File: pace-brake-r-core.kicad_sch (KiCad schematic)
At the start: 15 parts, among them Q1 AOD4184, Q2 AOD4184, U1 EG2131, U2 TL432AIDBZR

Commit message: updated notes in schematic
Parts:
- C1: footprint (none) -> Capacitor_SMD:C_0402_1005Metric
- D2: footprint (none) -> LED_SMD:LED_0805_2012Metric
- R1, R2, R3, R5, R6: footprint (none) -> Resistor_SMD:R_0402_1005Metric
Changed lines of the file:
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@@
 	)
 	(image
-		(at 146.05 27.94)
+		(at 142.24 -15.24)
 		(data "iVBORw0KGgoAAAANSUhEUgAACjsAAAP9CAYAAADR000DAAAABHNCSVQICAgIfAhkiAAAIABJREFU"
 			"eJzs3emXbFd55/nfs88QkXdEQkgIhEGAJYEE2MYYbLDAgO0qXMYuqHJNtld3Vy/36nrXq1cPf0S/"
@@
 	)
 	(image
-		(at -8.89 127)
+		(at -48.26 57.15)
 		(data "iVBORw0KGgoAAAANSUhEUgAAA7oAAAJ9CAYAAAAbng7VAAAABHNCSVQICAgIfAhkiAAAIABJREFU"
 			"eJzs3X9YVHXe//EXijoU5GC2DZspmFaYlrB2Kaxed2CtOebeBrfuBumWo96rWHsX6Fa6fnddrE2l"
@@
 			)
 		)
-		(property "Footprint" ""
+		(property "Footprint" "Resistor_SMD:R_0402_1005Metric"
 			(at 64.516 122.174 90)
 			(hide yes)
@@
 			)
 		)
-		(property "Footprint" ""
+		(property "Footprint" "LED_SMD:LED_0805_2012Metric"
 			(at 238.76 113.03 0)
 			(hide yes)
@@
 			)
 		)
-		(property "Footprint" ""
+		(property "Footprint" "Resistor_SMD:R_0402_1005Metric"
 			(at 162.814 129.794 90)
 			(hide yes)
@@
 			)
 		)
-		(property "Footprint" ""
+		(property "Footprint" "Resistor_SMD:R_0402_1005Metric"
 			(at 117.094 159.004 90)
 			(hide yes)
@@
 			)
 		)
-		(property "Footprint" ""
+		(property "Footprint" "Resistor_SMD:R_0402_1005Metric"
 			(at 226.314 127.254 90)
 			(hide yes)
@@
 			)
 		)
-		(property "Footprint" ""
+		(property "Footprint" "Resistor_SMD:R_0402_1005Metric"
 			(at 92.456 122.174 90)
 			(hide yes)
@@
 			)
 		)
-		(property "Footprint" ""
+		(property "Footprint" "Capacitor_SMD:C_0402_1005Metric"
 			(at 129.54 109.22 0)
 			(hide yes)

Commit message: Last version with LED indicator
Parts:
- removed D1: MBRD30100CT, imported-project-library:TO-252-2_L6.6-W6.1-P4.57-LS9.9-BR-CW, symbol imported-project-library:MBRD30100CT
- removed R7: ~, symbol Device:R
- added C16: 33nF, Capacitor_SMD:C_0402_1005Metric, symbol Device:C_Small
- added C17: 100uF 16v, Capacitor_SMD:C_Elec_6.3x7.7, symbol Device:C_Polarized
- added C2: 10uF, Capacitor_SMD:C_0402_1005Metric, symbol Device:C_Small
- added C35: 2.2uF, Capacitor_SMD:C_1210_3225Metric, symbol Device:C_Small
- added C5: 47uF 100V, Capacitor_SMD:CP_Elec_10x10, symbol Device:C_Small
- added D4, D5: SS310, Diode_SMD:D_SMA, symbol Diode:SS310
- added J2, J3: Conn_01x02_Socket, Connector_AMASS:AMASS_XT30U-F_1x02_P5.0mm_Vertical, symbol Connector:Conn_01x02_Socket
- added L1: 220uH @ 1A, imported-project-library:IND-TH_BD9.0-P5.00-D0.7, symbol imported-project-library:RLB9012-221KL
- added R14: 11k008 1%, Resistor_SMD:R_0402_1005Metric, symbol Device:R_US
- added R15: 1k370 1%, Resistor_SMD:R_0402_1005Metric, symbol Device:R_US
- added U3: XL7015E1, imported-project-library:TO-252-5_L6.6-W5.8-P1.27-TL, symbol imported-project-library:XL7015E1
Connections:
- net +24V is gone; now on net +12V: D2.2 (A)
- net +12V: now also C16.1, C17.1, C2.1, L1.2, R14.1
- net GND: now also C17.2, C2.2, C35.2, C5.2, D4.2 (A), J3.2 (Pin_2), R15.2, U3.3 (GND), U3.6 (GND)
- net VDD: now also C35.1, C5.1, D5.1 (K), J2.1 (Pin_1), J3.1 (Pin_1), U3.1 (VIN)
- net at R1.2, R4.2: now also FB1.2, U2.1 (REF); no longer FB1.1, R5.1
- net at Q1.2 (D): now also D5.2 (A), J2.2 (Pin_2)
- new net: D4.1 (K), L1.1, U3.2 (SW)
- new net: C16.2, R14.2, R15.1, U3.4 (FB)
- new net: FB1.1, R5.1
- no-connect marks 5 -> 6
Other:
- note added: "Battery Input"
- note added: "Buck Regulator (48V -> 12V)"
- note added: "C_Decoupling"
- note added: "Hysteresis (1,000,000R)"
- note removed: "Hysteresis"

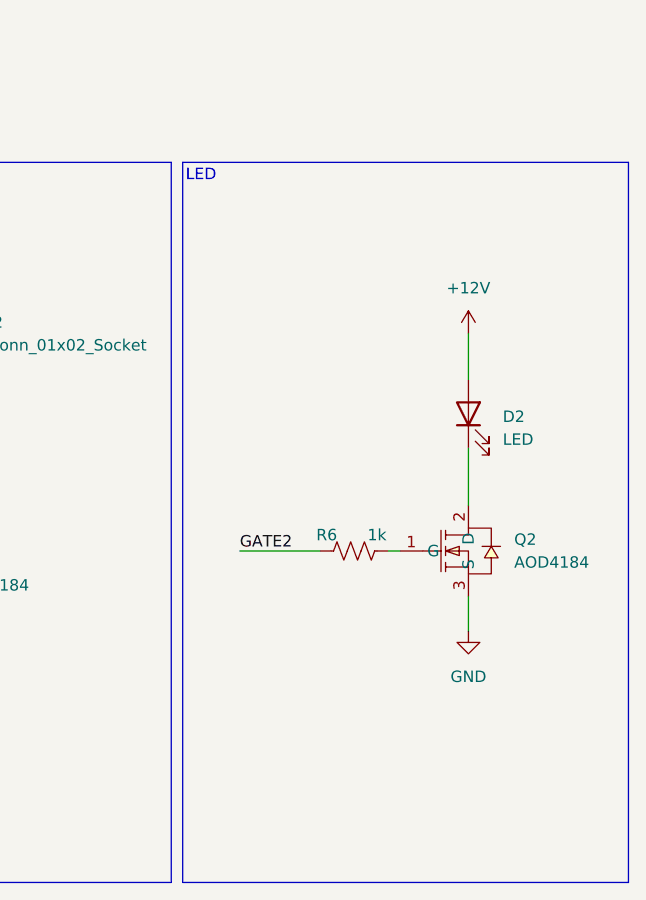
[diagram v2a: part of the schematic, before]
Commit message: Removed LED indicator, begin PCB layout
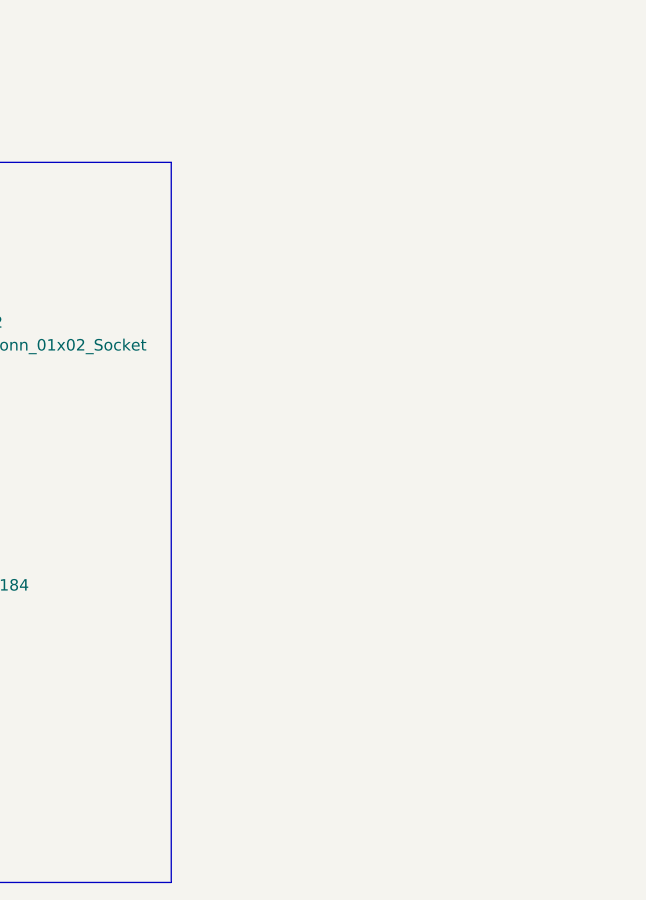
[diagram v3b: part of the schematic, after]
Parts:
- removed D2: LED, LED_SMD:LED_0805_2012Metric, symbol Device:LED
- removed Q2: AOD4184, imported-project-library:TO-252-2_L6.6-W6.1-P4.58-LS9.9-BR, symbol imported-project-library:AOD4184
- removed R6: 1k, Resistor_SMD:R_0402_1005Metric, symbol Device:R_US
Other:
- note removed: "LED"

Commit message: Continue PCB layout progress
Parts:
- added H1, H2: MountingHole, MountingHole:MountingHole_3.2mm_M3, symbol Mechanical:MountingHole
- renumbered R4 to R2, R2 to R4
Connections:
- net at FB1.2, R1.2, R2.2: now also R5.1; no longer U2.1 (REF)
- net at FB1.1: now also U2.1 (REF); no longer R5.1
- net GATE2: no longer names the net of R3.1, R5.2, U1.5 (LO)
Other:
- note added: "Adjustable Trimmer Pot."
- note added: "Mounting Holes"
- note removed: "Adjustable V Ref"
- moved on the sheet: J3

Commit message: schematic revision changes
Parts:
- removed J2, J3: Conn_01x02_Socket, Connector_AMASS:AMASS_XT30U-F_1x02_P5.0mm_Vertical, symbol Connector:Conn_01x02_Socket
- added BRAKE-R, CN1, CN2: XT30PW-M, imported-project-library:CONN-TH_XT30PW-M, symbol imported-project-library:XT30PW-M
- FB1: footprint (none) -> imported-project-library:L0603
- R14: value 11k008 1% -> 43k 1%
- R15: value 1k370 1% -> 5k 1%
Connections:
- net GND: now also BRAKE-R.3, BRAKE-R.4, CN1.1 (-), CN1.3, CN1.4, CN2.1 (-), CN2.3, CN2.4
- net VDD: now also BRAKE-R.2 (+), CN1.2 (+), CN2.2 (+)
- net comparator_out: now reaches R4.2, U1.3 (LIN), U2.2 (CAT)
- net at D5.2 (A), Q1.2 (D): now also BRAKE-R.1 (-)
- net V_in: now reaches FB1.1, U2.1 (REF)
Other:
- note added: "Power Conn"
- note removed: "Battery Input"
- note removed: "Output"
- moved on the sheet: FB1, H1, H2, R4, R5
